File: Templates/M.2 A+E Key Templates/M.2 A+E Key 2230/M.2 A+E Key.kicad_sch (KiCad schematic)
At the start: 2 parts

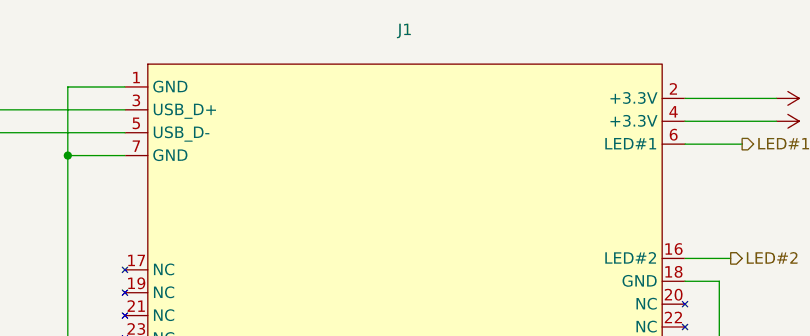
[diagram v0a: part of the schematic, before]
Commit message: updated names on symbols
updated the "Value" field in the m.2 symbols so the name of the connector is shown in your schematic.

updated a few templates with new m.2 symbols
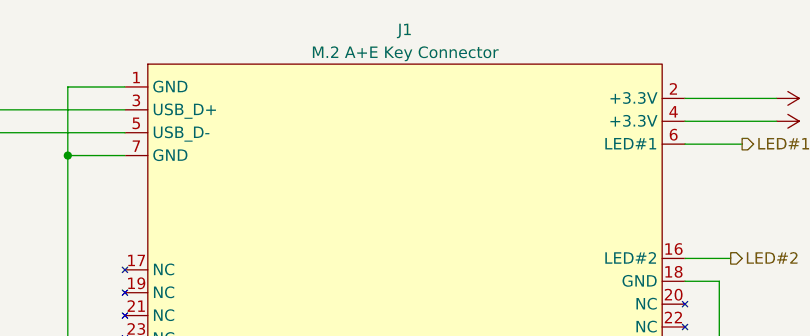
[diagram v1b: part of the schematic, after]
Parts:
- J1: value ~ -> M.2 A+E Key Connector
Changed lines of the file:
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@@
 			)
 		)
-		(property "Value" "~"
+		(property "Value" "M.2 A+E Key Connector"
 			(at 126.365 45.72 0)
 			(effects
